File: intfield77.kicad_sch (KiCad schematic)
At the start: 20 parts, among them J1 USB_C_Receptacle_USB2.0, SW1 RESET, SW2 BOOT, U1 STM32F072C8Tx, U2 SRV05-4, U3 XC6206PxxxMR

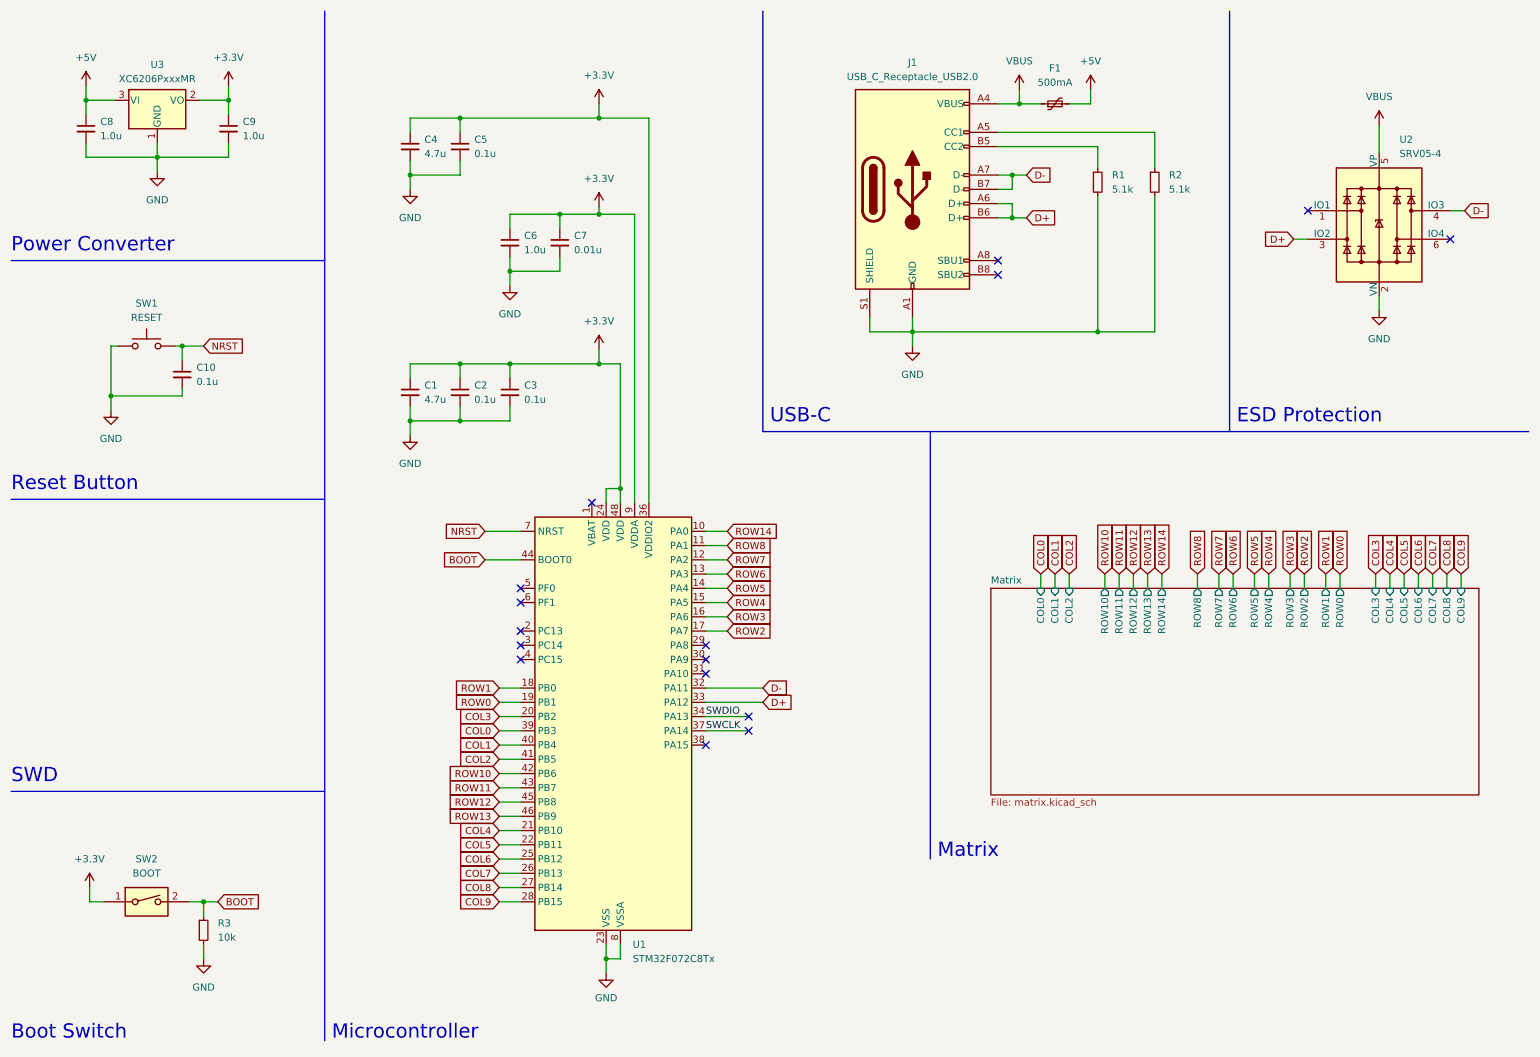
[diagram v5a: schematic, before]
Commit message: Shuffled MCU pins and realigned schema to 50 mils, but USB connector is not connected.
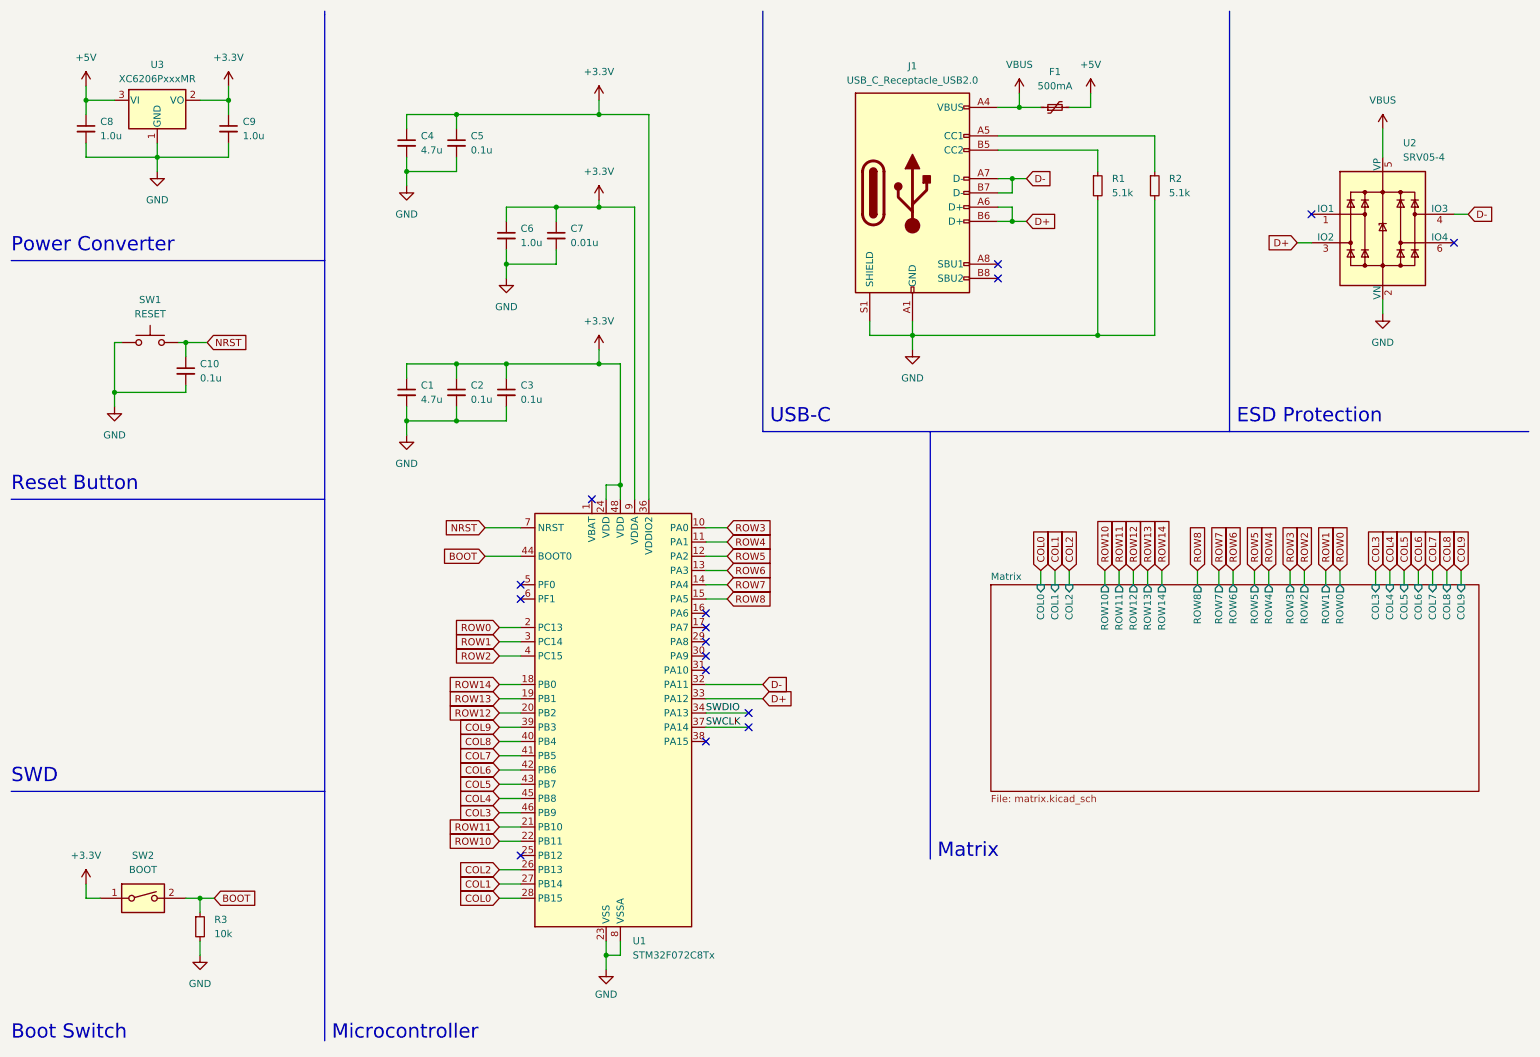
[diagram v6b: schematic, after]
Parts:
- C1: footprint Capacitor_SMD:C_0805_2012Metric -> Connector_USB:USB_C_Receptacle_HRO_TYPE-C-31-M-12
- J1: footprint Type-C:HRO-TYPE-C-31-M-12-Assembly -> Type-C:HRO-TYPE-C-31-M-12
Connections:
- net COL0: now also U1.28 (PB15); no longer U1.39 (PB3)
- net COL1: now also U1.27 (PB14); no longer U1.40 (PB4)
- net COL2: now also U1.26 (PB13); no longer U1.41 (PB5)
- net COL3: now also U1.46 (PB9); no longer U1.20 (PB2)
- net COL4: now also U1.45 (PB8); no longer U1.21 (PB10)
- net COL5: now also U1.43 (PB7); no longer U1.22 (PB11)
- net COL6: now also U1.42 (PB6); no longer U1.25 (PB12)
- net COL7: now also U1.41 (PB5); no longer U1.26 (PB13)
- net COL8: now also U1.40 (PB4); no longer U1.27 (PB14)
- net COL9: now also U1.39 (PB3); no longer U1.28 (PB15)
- net ROW0: now also U1.2 (PC13); no longer U1.19 (PB1)
- net ROW1: now also U1.3 (PC14); no longer U1.18 (PB0)
- net ROW10: now also U1.22 (PB11); no longer U1.42 (PB6)
- net ROW11: now also U1.21 (PB10); no longer U1.43 (PB7)
- net ROW12: now also U1.20 (PB2); no longer U1.45 (PB8)
- net ROW13: now also U1.19 (PB1); no longer U1.46 (PB9)
- net ROW14: now also U1.18 (PB0); no longer U1.10 (PA0)
- net ROW2: now also U1.4 (PC15); no longer U1.17 (PA7)
- net ROW3: now also U1.10 (PA0); no longer U1.16 (PA6)
- net ROW4: now also U1.11 (PA1); no longer U1.15 (PA5)
- net ROW5: now also U1.12 (PA2); no longer U1.14 (PA4)
- net ROW7: now also U1.14 (PA4); no longer U1.12 (PA2)
- net ROW8: now also U1.15 (PA5); no longer U1.11 (PA1)
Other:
- moved on the sheet: C1, C10, C2, C3, C4, C5, C6, C7, F1, J1, R1, R2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

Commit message: Changed USB-C and reset button symbols and footprints, still problems.
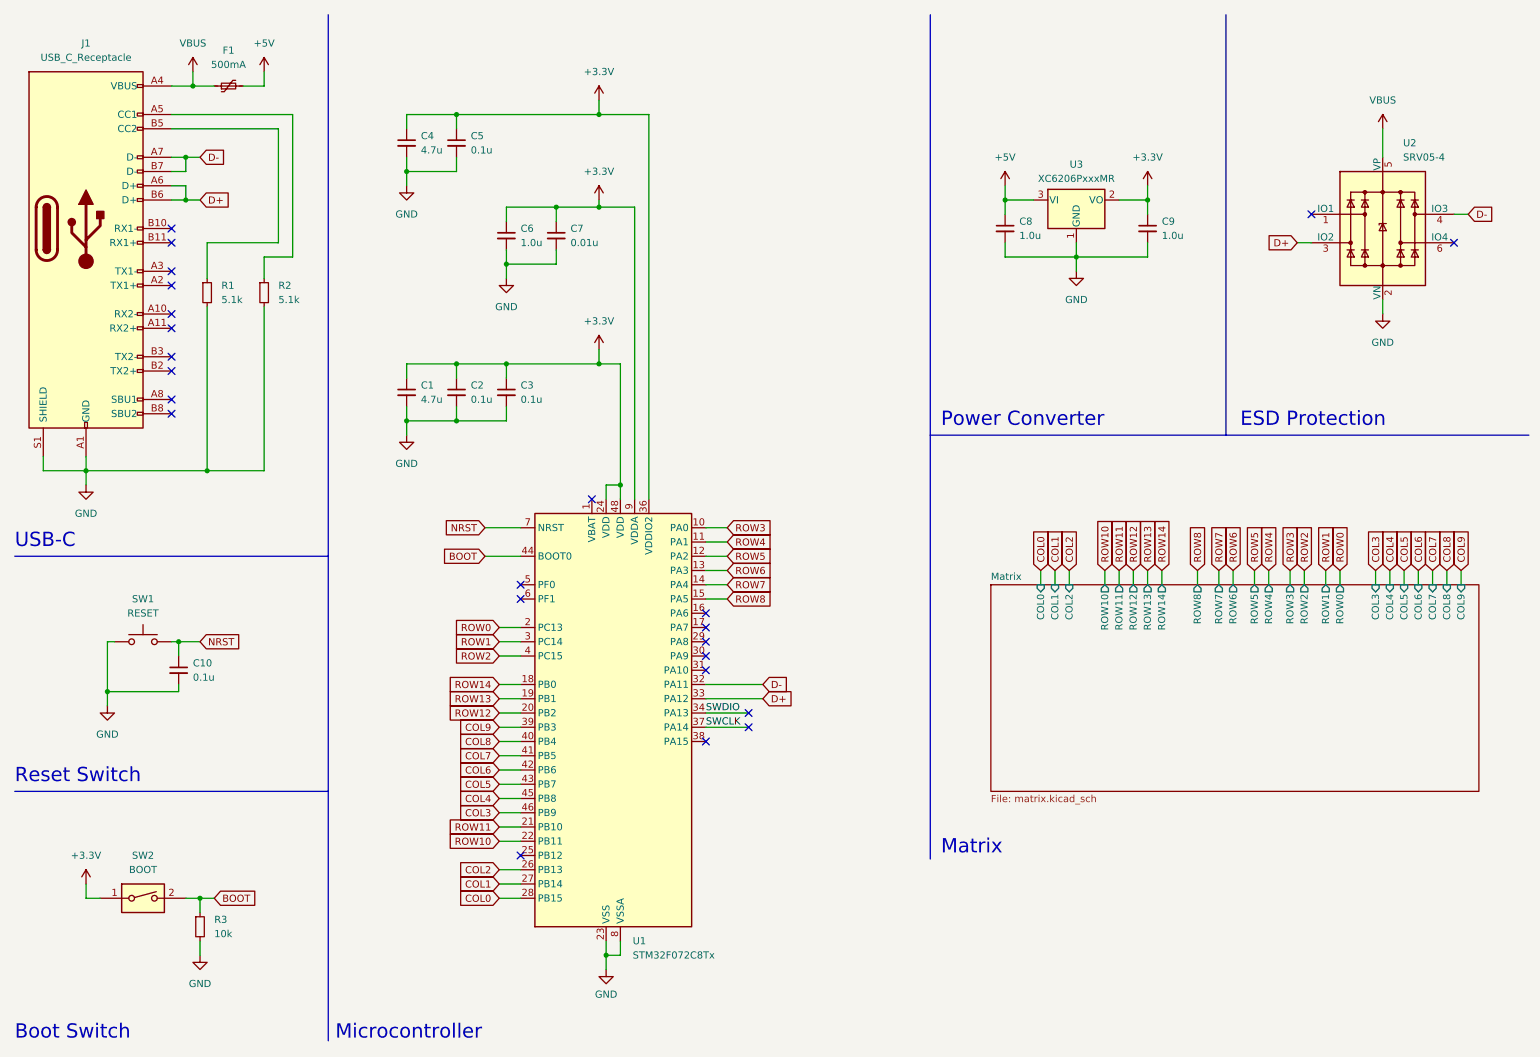
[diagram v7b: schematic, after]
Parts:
- removed J1: USB_C_Receptacle_USB2.0, Type-C:HRO-TYPE-C-31-M-12, symbol Connector:USB_C_Receptacle_USB2.0
- added J1: USB_C_Receptacle, Connector_USB:USB_C_Receptacle_HRO_TYPE-C-31-M-12, symbol Connector:USB_C_Receptacle
- C1: footprint Connector_USB:USB_C_Receptacle_HRO_TYPE-C-31-M-12 -> Capacitor_SMD:C_0805_2012Metric
- SW1: footprint random-keyboard-parts:SKQGADE010 -> Button_Switch_SMD:SW_Push_SPST_NO_Alps_SKRK
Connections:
- net D+: now also J1.A6 (D+), J1.B6 (D+)
- net D-: now also J1.A7 (D-), J1.B7 (D-)
- net GND: now also J1.A1 (GND), J1.A12 (GND), J1.B1 (GND), J1.B12 (GND), J1.S1 (SHIELD)
- net VBUS: now also J1.A4 (VBUS), J1.A9 (VBUS), J1.B4 (VBUS), J1.B9 (VBUS)
- net at R1.1: now also J1.B5 (CC2)
- net at R2.1: now also J1.A5 (CC1)
- no-connect marks 16 -> 24
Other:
- note added: "Reset Switch"
- note removed: "Reset Button"
- note removed: "SWD"
- moved on the sheet: C10, C8, C9, F1, R1, R2, SW1, U3

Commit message: Fixed it, I think.
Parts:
- J1: symbol Connector:USB_C_Receptacle -> Connector:USB_C_Receptacle_USB2.0
- SW1: footprint Button_Switch_SMD:SW_Push_SPST_NO_Alps_SKRK -> Button_Switch_SMD:SW_SPST_SKQG_WithStem
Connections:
- no-connect marks 24 -> 16
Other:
- moved on the sheet: C10, F1, R1, R2, SW1
